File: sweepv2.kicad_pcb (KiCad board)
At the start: 2 copper layers, 216.9 x 86.9 mm, 51 parts, among them J1 AudioJack4dpb, J2 AudioJack4dpb, SW10 SW_Push, SW11 SW_Push, SW11_r1 SW_Push, SW12 SW_Push, SW12_r1 SW_Push, SW13_r1 SW_Push, SW14 SW_Push, SW15 SW_Push, SW15_r1 SW_Push, SW16 SW_Push, SW16_r1 SW_Push, SW17 SW_Push, SW17_r1 SW_Push, SW18 SW_Push, SW18_r1 SW_Push, SW2 SW_Push, SW20 SW_Push, SW20_r1 SW_Push, SW21 SW_Push, SW21_r1 SW_Push, SW2_r1 SW_Push, SW3 SW_Push, SW3_r1 SW_Push, SW4 SW_Push, SW4_r1 SW_Push, SW5 SW_Push, SW5_r1 SW_Push, SW6 SW_Push, SW6_r1 SW_Push, SW7_r1 SW_Push, SW8 SW_Push, SW8_r1 SW_Push, SW9 SW_Push, SW9_r1 SW_Push, U1 ProMicro-kbd, U2 ProMicro-kbd

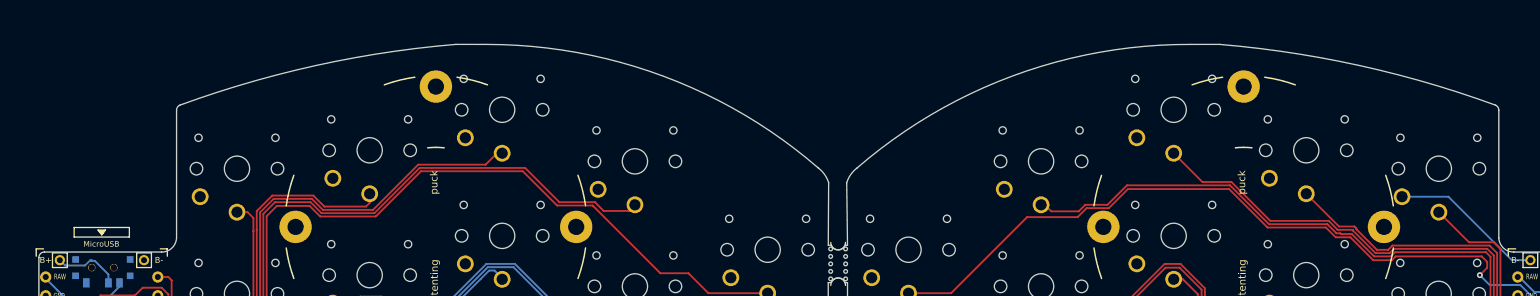
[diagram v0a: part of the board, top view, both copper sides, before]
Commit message: Change cutout lines for PCB
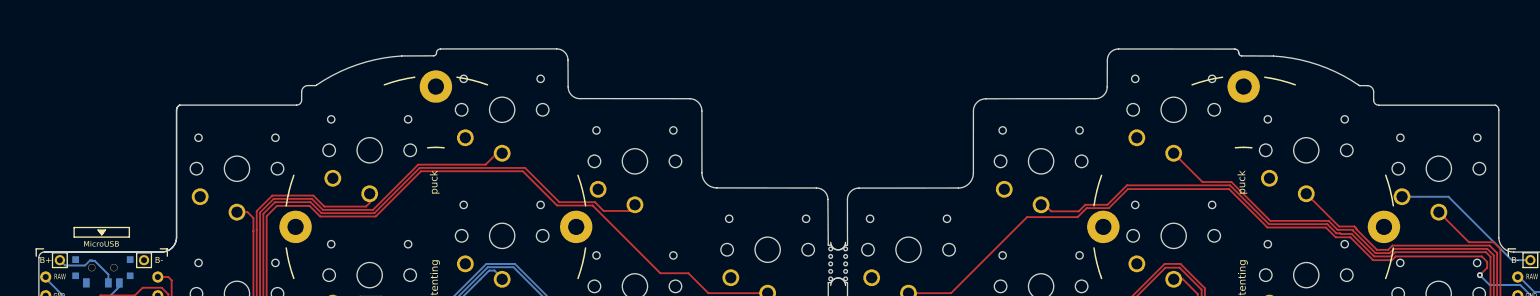
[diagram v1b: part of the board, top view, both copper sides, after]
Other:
- board size 216.9 x 86.9 mm -> 216.9 x 86.2 mm

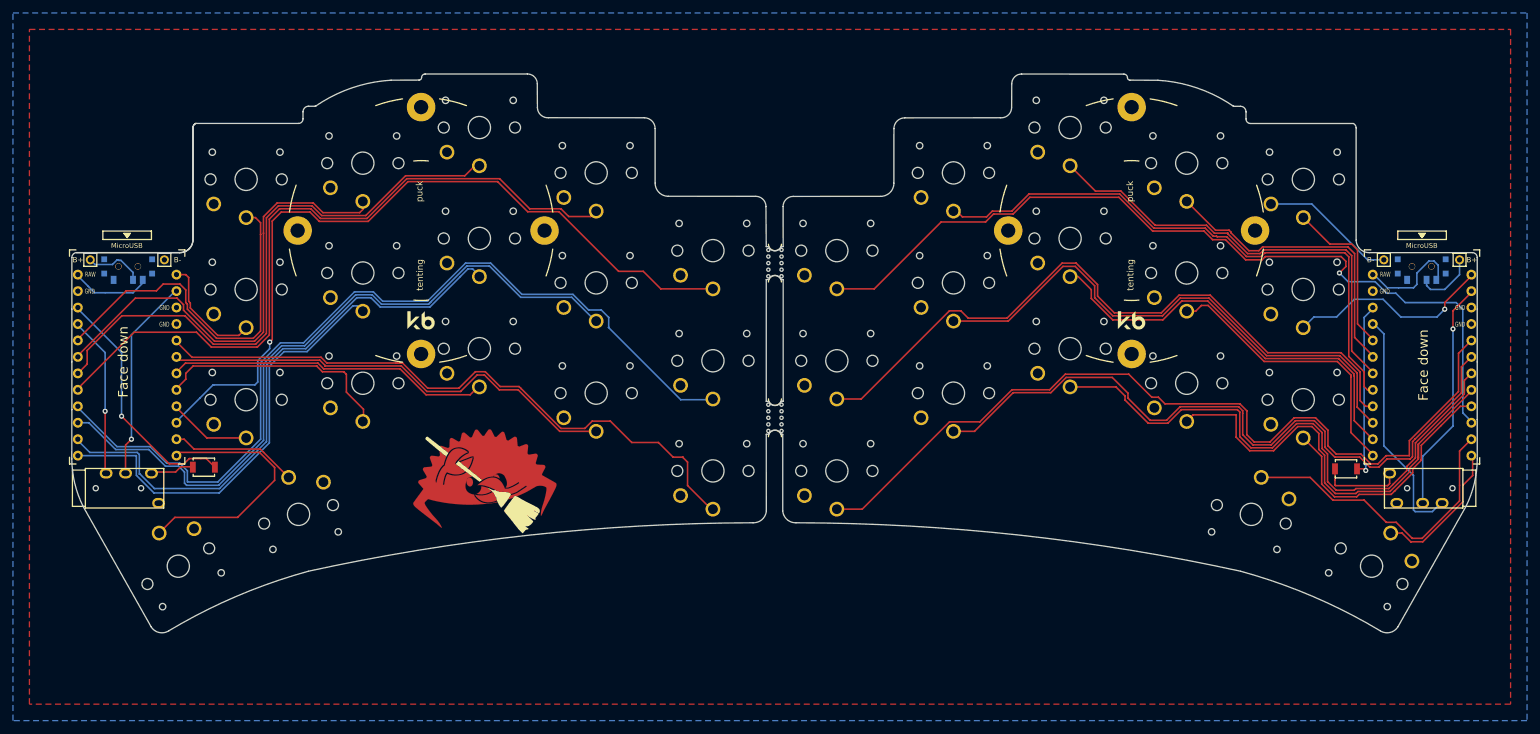
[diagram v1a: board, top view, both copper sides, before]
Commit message: Mirrored edge.cuts, kicad not recognising them as closed
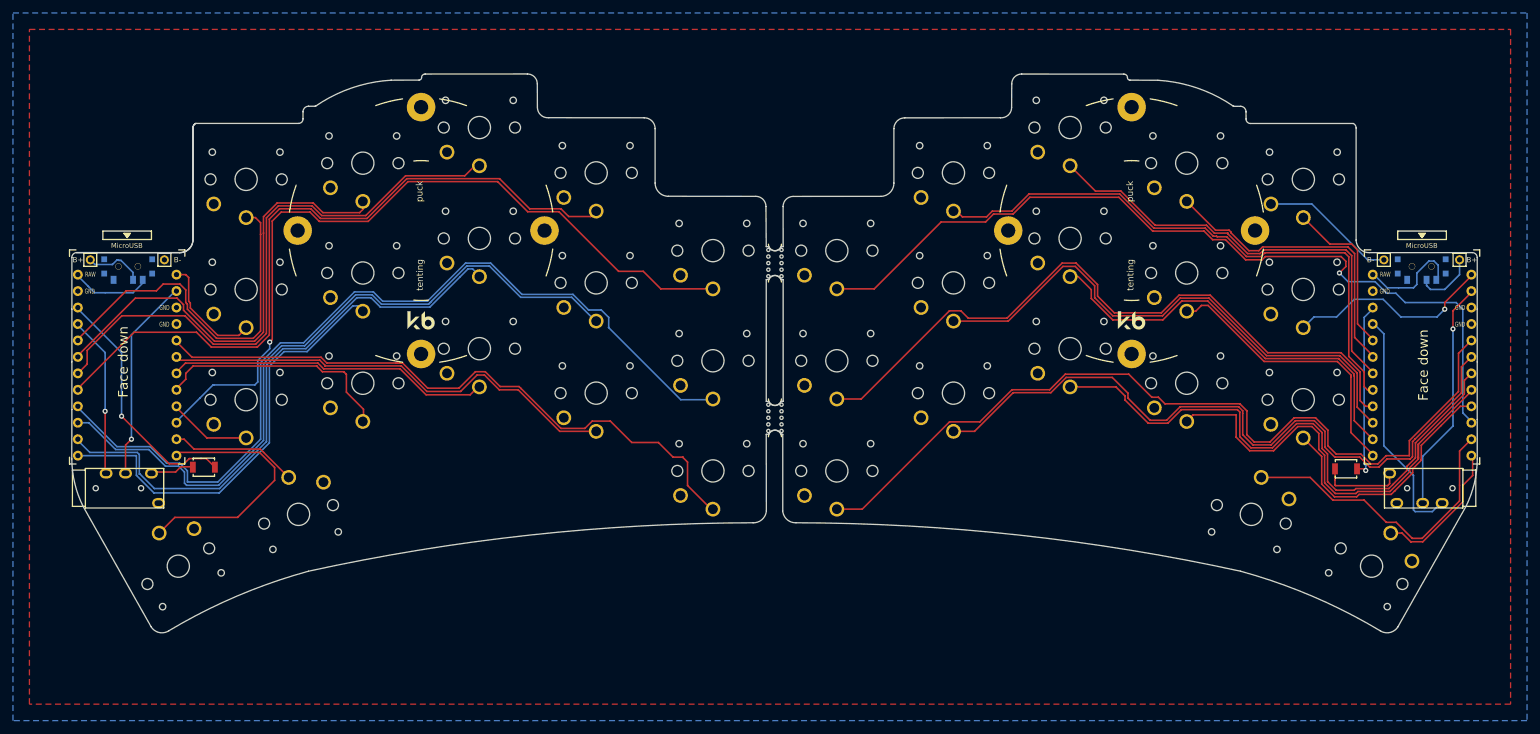
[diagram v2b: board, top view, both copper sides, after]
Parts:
- removed G***: LOGO, Kailh:ferris_broom

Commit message: started changing cutout, no errors
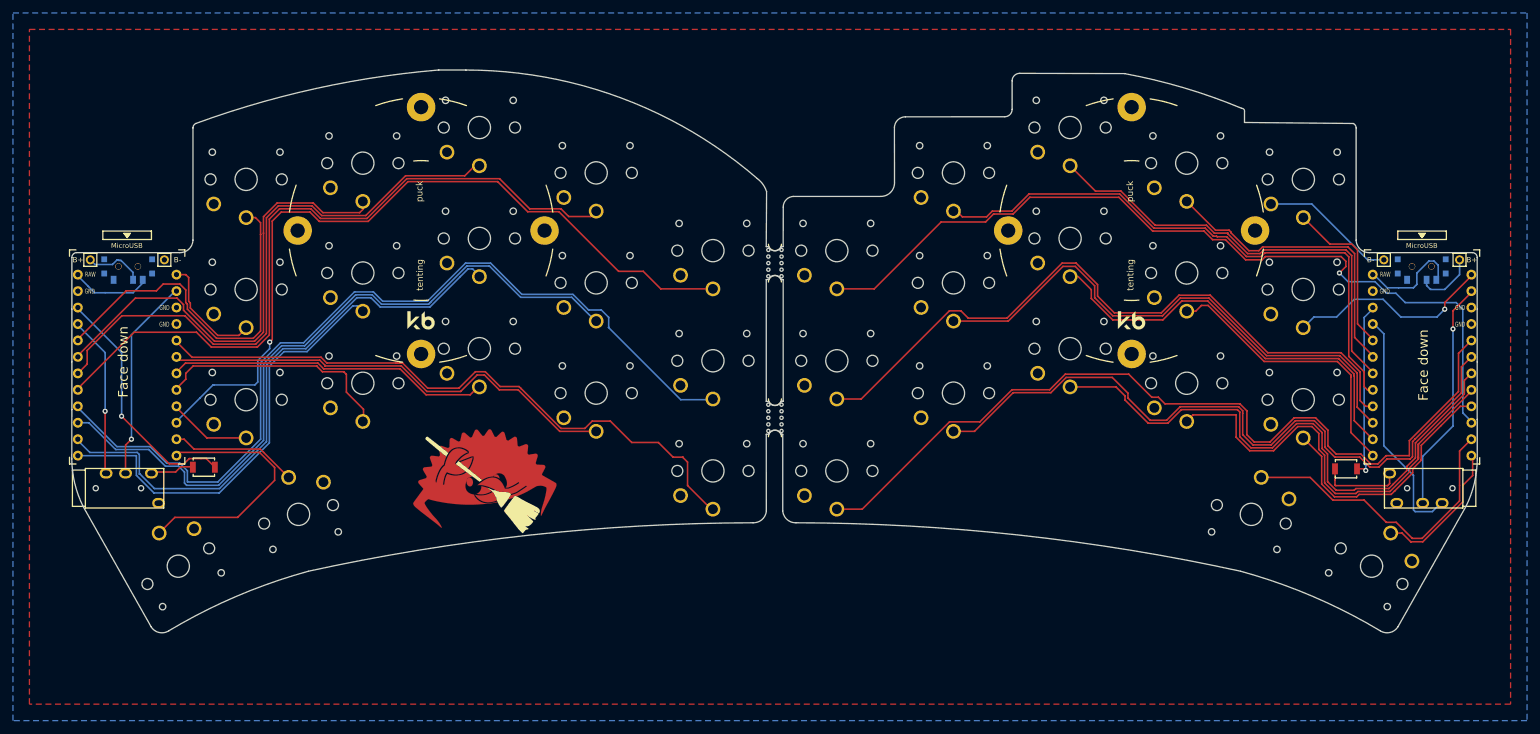
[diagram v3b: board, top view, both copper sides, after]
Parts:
- added G***: LOGO, Kailh:ferris_broom, F.Cu at (84.1, 85.3)
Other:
- board size 216.9 x 86.2 mm -> 216.9 x 86.9 mm
